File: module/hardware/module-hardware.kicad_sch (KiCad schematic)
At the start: 18 parts

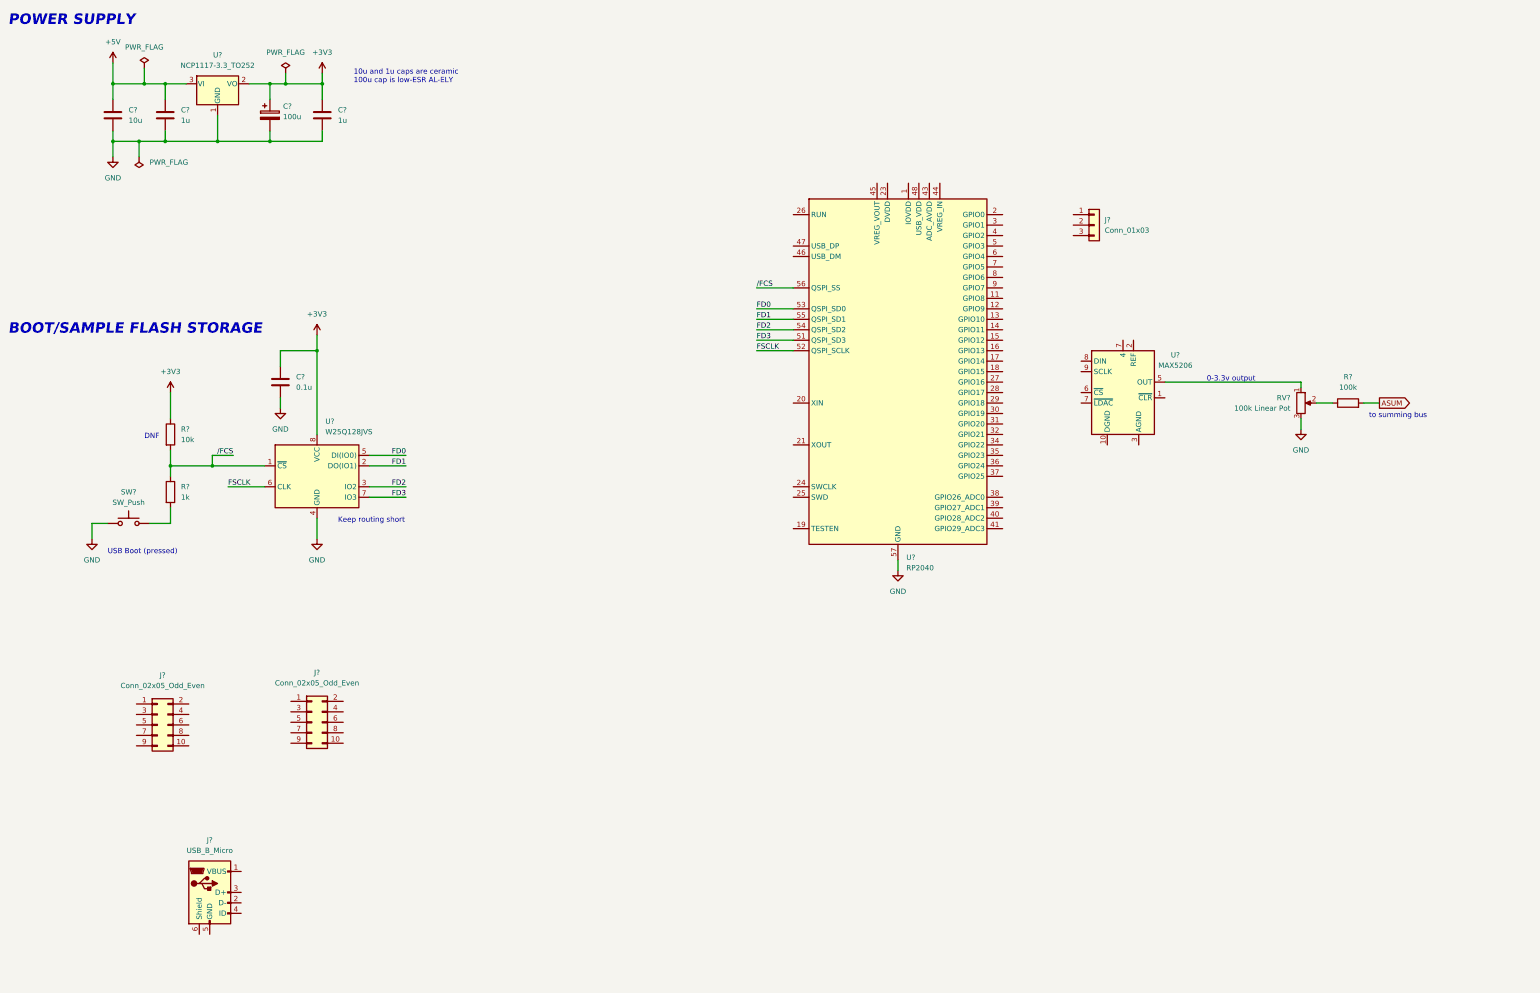
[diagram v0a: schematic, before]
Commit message: Add USB, XTAL, ADC headers, MCU bypass caps, reset
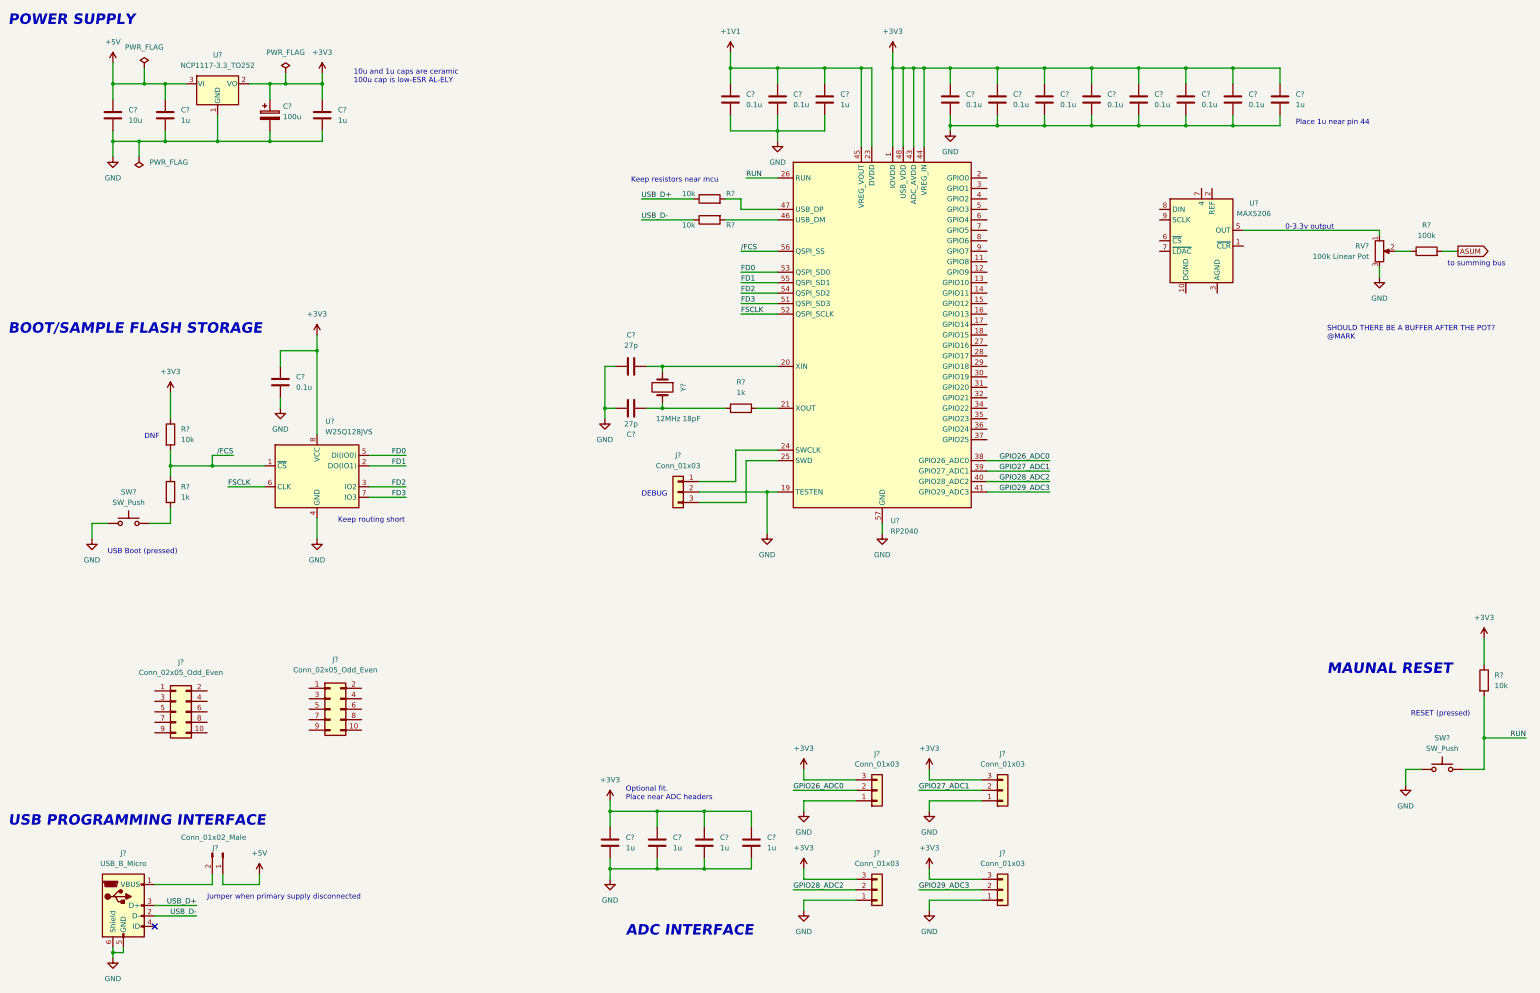
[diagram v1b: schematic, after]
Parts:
- removed J?: Conn_01x03, symbol Connector_Generic:Conn_01x03
- added C? (x6): 1u, symbol Device:C
- added C? (x2): 27p, symbol Device:C
- added C? (x9): 0.1u, symbol Device:C
- added J? (x5): Conn_01x03, symbol Connector_Generic:Conn_01x03
- added J?: Conn_01x02_Male, symbol Connector:Conn_01x02_Male
- added R? (x3): 10k, symbol Device:R
- added R?: 1k, symbol Device:R
- added SW?: SW_Push, symbol Switch:SW_Push
- added Y?: 12MHz 18pF, symbol Device:Crystal
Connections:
- net +3V3: now also U?.1 (IOVDD), U?.10 (IOVDD), U?.22 (IOVDD), U?.33 (IOVDD), U?.42 (IOVDD), U?.43 (ADC_AVDD), U?.44 (VREG_IN), U?.48 (USB_VDD), U?.49 (IOVDD), C?.1, C?.1, C?.1, C?.1, C?.1, C?.1, C?.1, C?.1, C?.1, C?.1, C?.1, C?.1, J?.3 (Pin_3), J?.3 (Pin_3), J?.3 (Pin_3), J?.3 (Pin_3), R?.1
- net +5V: now also J?.1 (Pin_1)
- net GND: now also J?.5 (GND), J?.6 (Shield), U?.19 (TESTEN), C?.1, C?.2, C?.2, C?.2, C?.2, C?.2, C?.2, C?.2, C?.2, C?.2, C?.2, C?.2, C?.2, C?.2, C?.2, C?.2, C?.2, J?.1 (Pin_1), J?.1 (Pin_1), J?.1 (Pin_1), J?.1 (Pin_1), J?.2 (Pin_2), SW?.1
- net at J?.1 (VBUS): now also J?.2 (Pin_2)
- net USB_D-: now reaches J?.2 (D-)
- net USB_D-: now also R?.1
- net USB_D+: now reaches J?.3 (D+)
- net USB_D+: now also R?.1
- net at U?.20 (XIN): now also C?.2, Y?.1
- net at U?.21 (XOUT): now also R?.2
- net +1V1: now reaches U?.23 (DVDD), U?.50 (DVDD)
- net +1V1: now also U?.45 (VREG_VOUT), C?.1, C?.1, C?.1
- net at U?.24 (SWCLK): now also J?.1 (Pin_1)
- net at U?.25 (SWD): now also J?.3 (Pin_3)
- net RUN: now reaches U?.26 (RUN)
- net RUN: now also R?.2, SW?.2
- net GPIO26_ADC0: now reaches U?.38 (GPIO26_ADC0)
- net GPIO26_ADC0: now also J?.2 (Pin_2)
- net GPIO27_ADC1: now reaches U?.39 (GPIO27_ADC1)
- net GPIO27_ADC1: now also J?.2 (Pin_2)
- net GPIO28_ADC2: now reaches U?.40 (GPIO28_ADC2)
- net GPIO28_ADC2: now also J?.2 (Pin_2)
- net GPIO29_ADC3: now reaches U?.41 (GPIO29_ADC3)
- net GPIO29_ADC3: now also J?.2 (Pin_2)
- net at U?.46 (USB_DM): now also R?.2
- net at U?.47 (USB_DP): now also R?.2
- new net: C?.1, R?.1, Y?.2
- no-connect marks 0 -> 1
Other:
- note added: "ADC INTERFACE"
- note added: "DEBUG"
- note added: "Jumper when primary supply disconnected"
- note added: "Keep resistors near mcu"
- note added: "MAUNAL RESET"
- note added: "Optional fit. Place near ADC headers"
- note added: "Place 1u near pin 44"
- note added: "RESET (pressed)"
- note added: "SHOULD THERE BE A BUFFER AFTER THE POT? @MARK"
- note added: "USB PROGRAMMING INTERFACE"
- moved on the sheet: J?, R?, RV?, U?

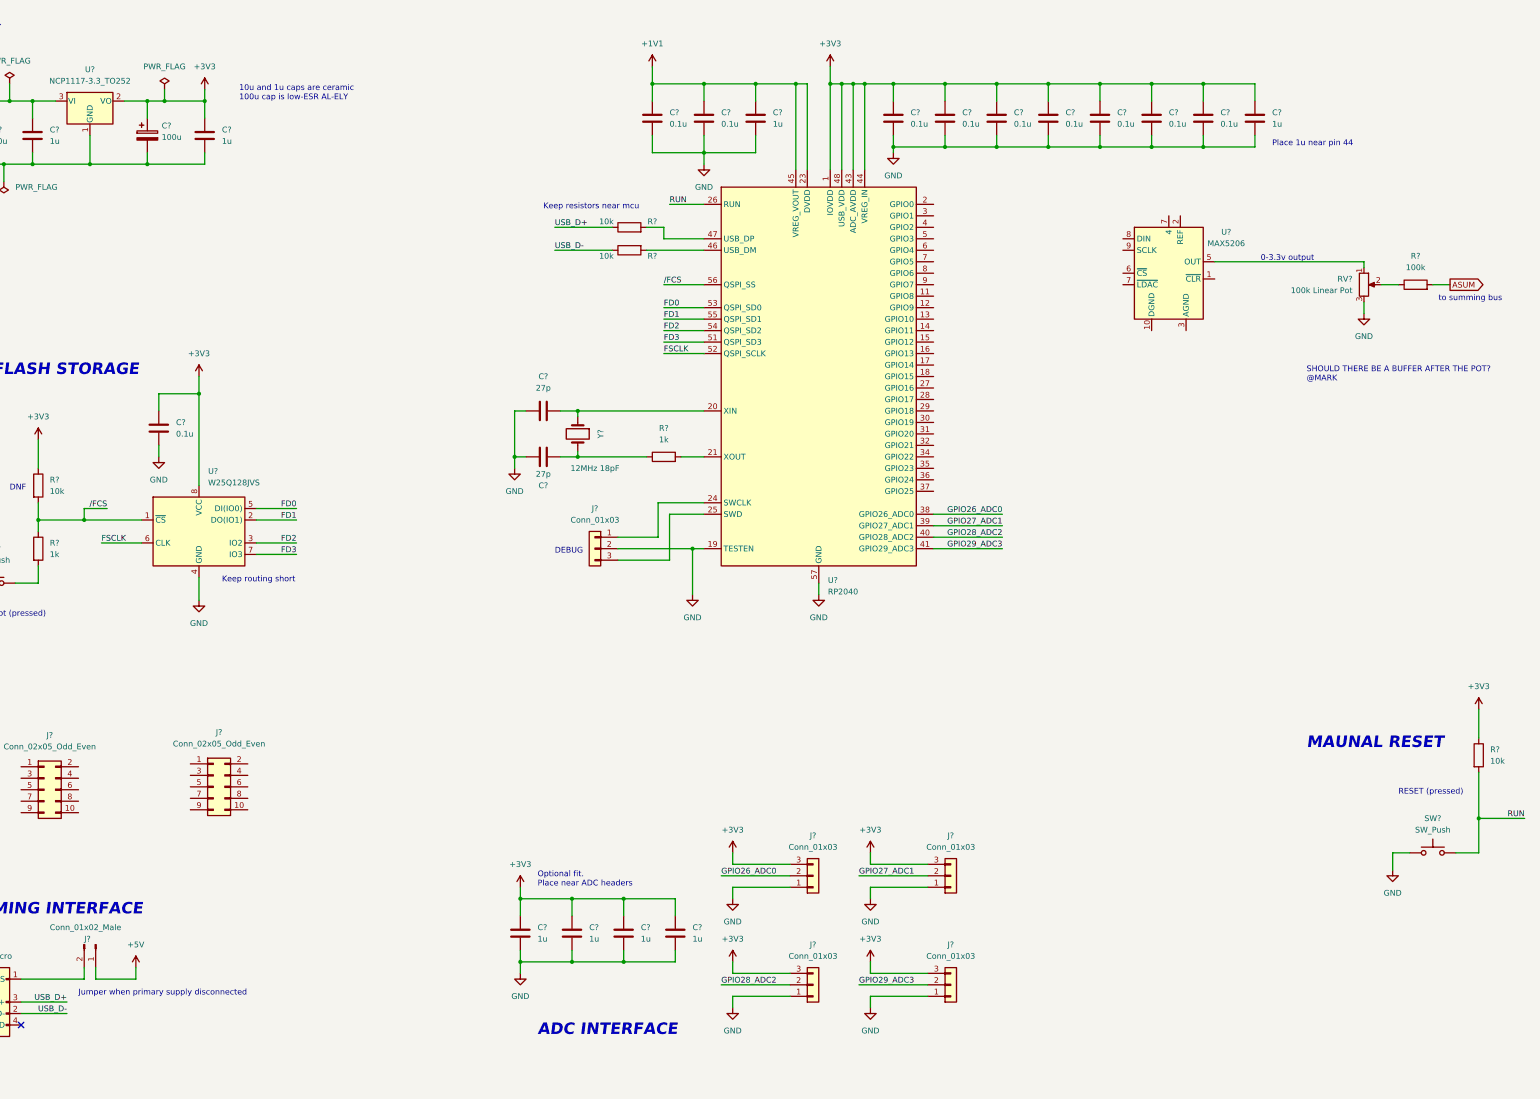
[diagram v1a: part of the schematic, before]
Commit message: Add DAC connections
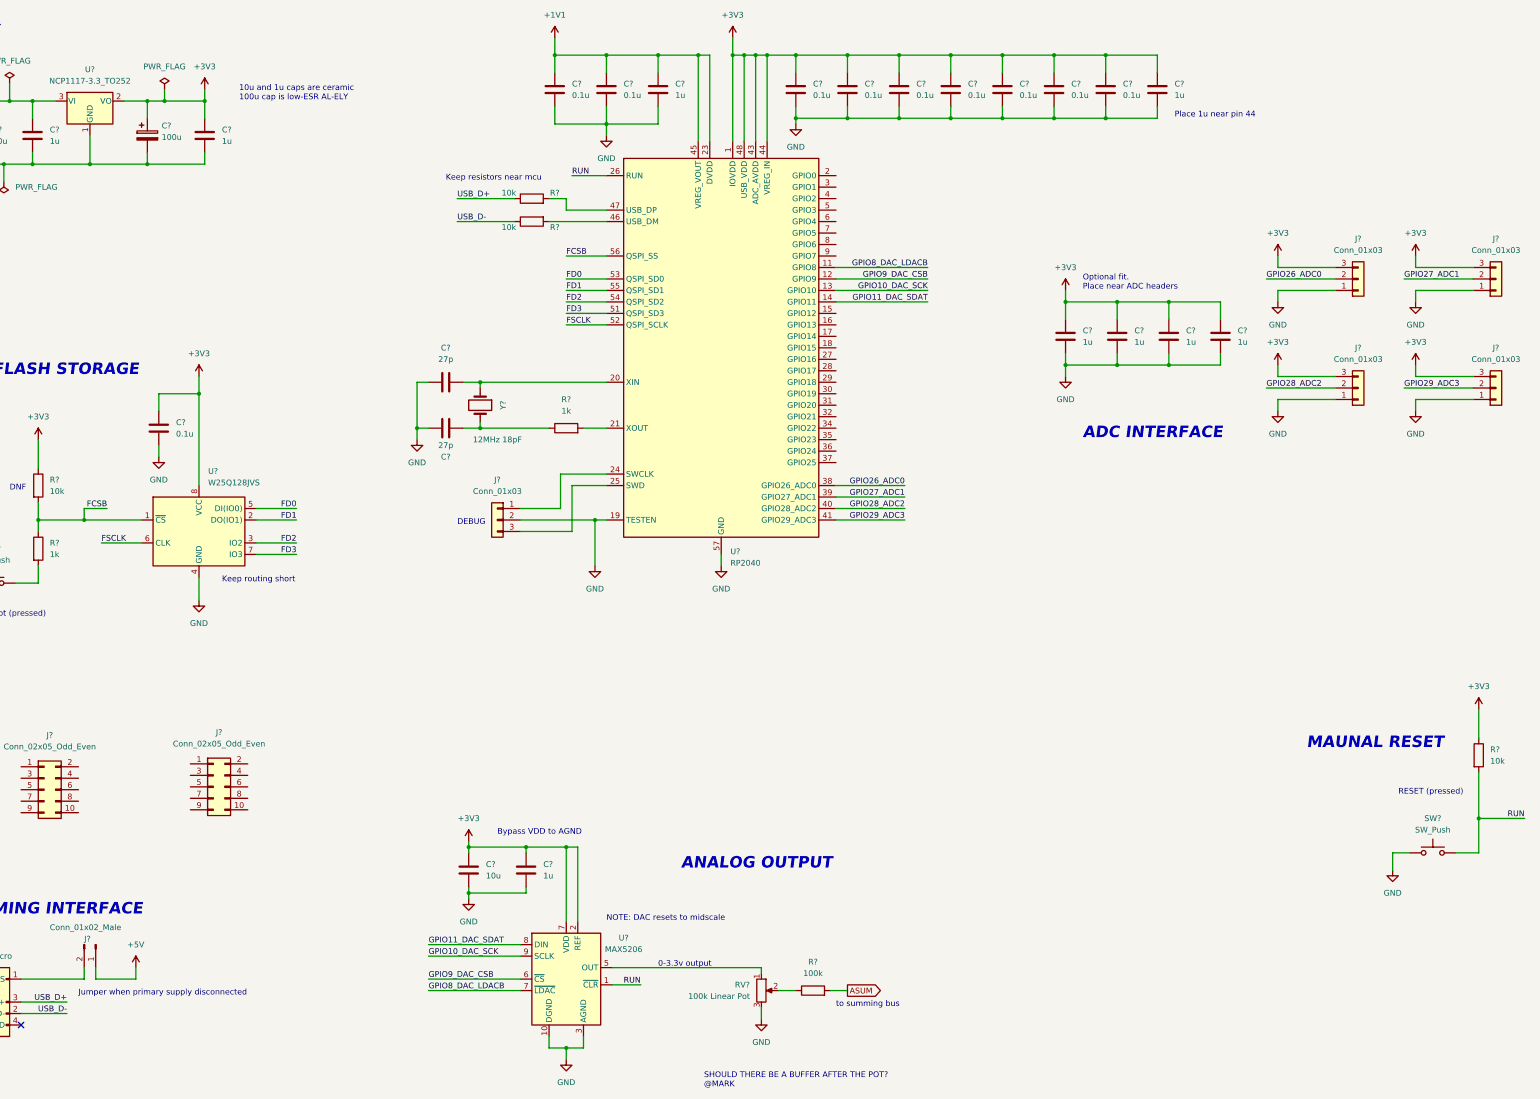
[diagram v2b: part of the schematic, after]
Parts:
- added C?: 1u, symbol Device:C
- added C?: 10u, symbol Device:C
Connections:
- net +3V3: now also U?.2 (REF), U?.7 (~{LDAC}), C?.1, C?.1
- net GND: now also U?.10 (DGND), U?.3 (AGND), C?.2, C?.2
- net RUN: now also U?.1 (~{CLR})
- net GPIO8_DAC_LDACB: now reaches U?.11 (GPIO8)
- net GPIO8_DAC_LDACB: now also U?.7 (~{LDAC})
- net GPIO9_DAC_CSB: now reaches U?.12 (GPIO9)
- net GPIO9_DAC_CSB: now also U?.6 (~{CS})
- net GPIO10_DAC_SCK: now reaches U?.13 (GPIO10)
- net GPIO10_DAC_SCK: now also U?.9 (SCLK)
- net GPIO11_DAC_SDAT: now reaches U?.14 (GPIO11)
- net GPIO11_DAC_SDAT: now also U?.8 (DIN)
- net /FCS renamed FCSB
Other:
- note added: "ANALOG OUTPUT"
- note added: "Bypass VDD to AGND"
- note added: "NOTE: DAC resets to midscale"
- moved on the sheet: C?, J?, R?, RV?, U?, Y?
